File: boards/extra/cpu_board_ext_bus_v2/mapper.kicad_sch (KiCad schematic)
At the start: 3 parts, among them U2 74LS30, U7 74LS30, U8 ATF1502AS-7JX44

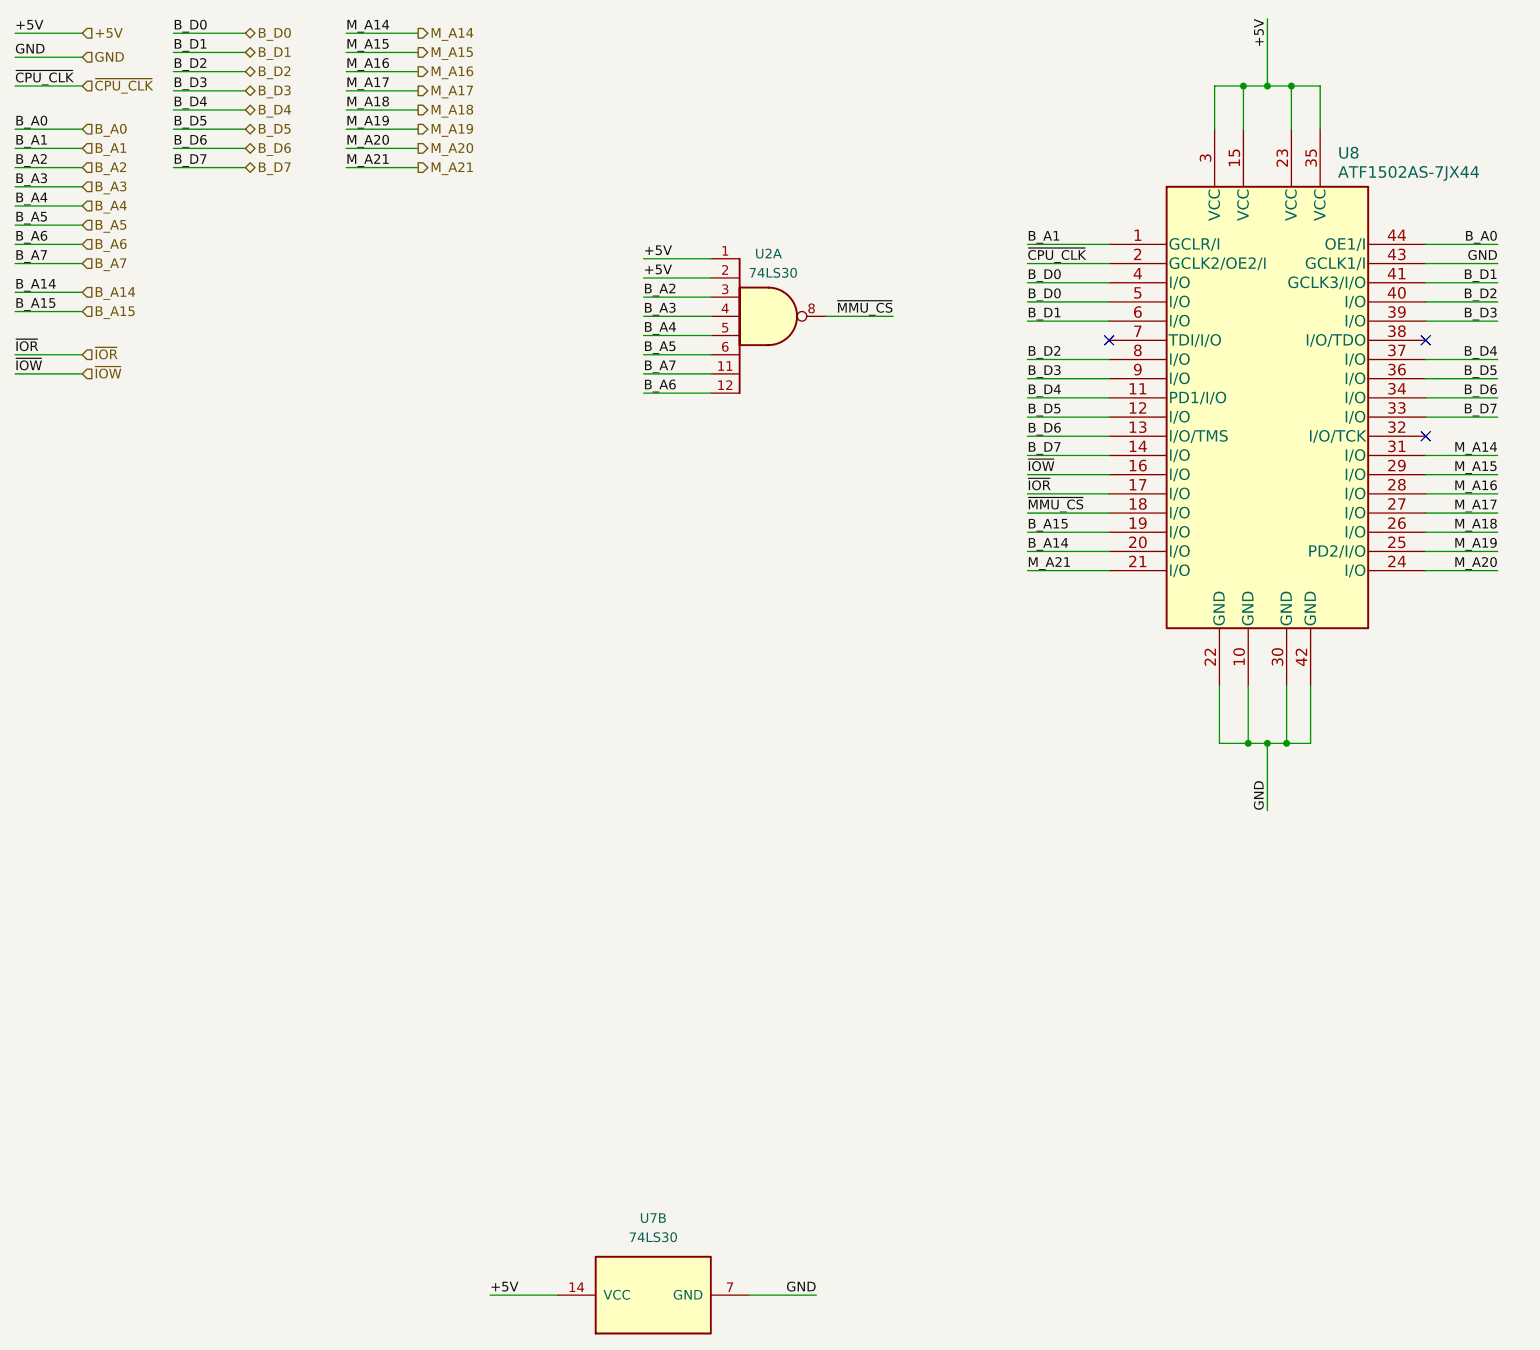
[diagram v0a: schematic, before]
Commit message: Updated CPU board V2 with extension bus
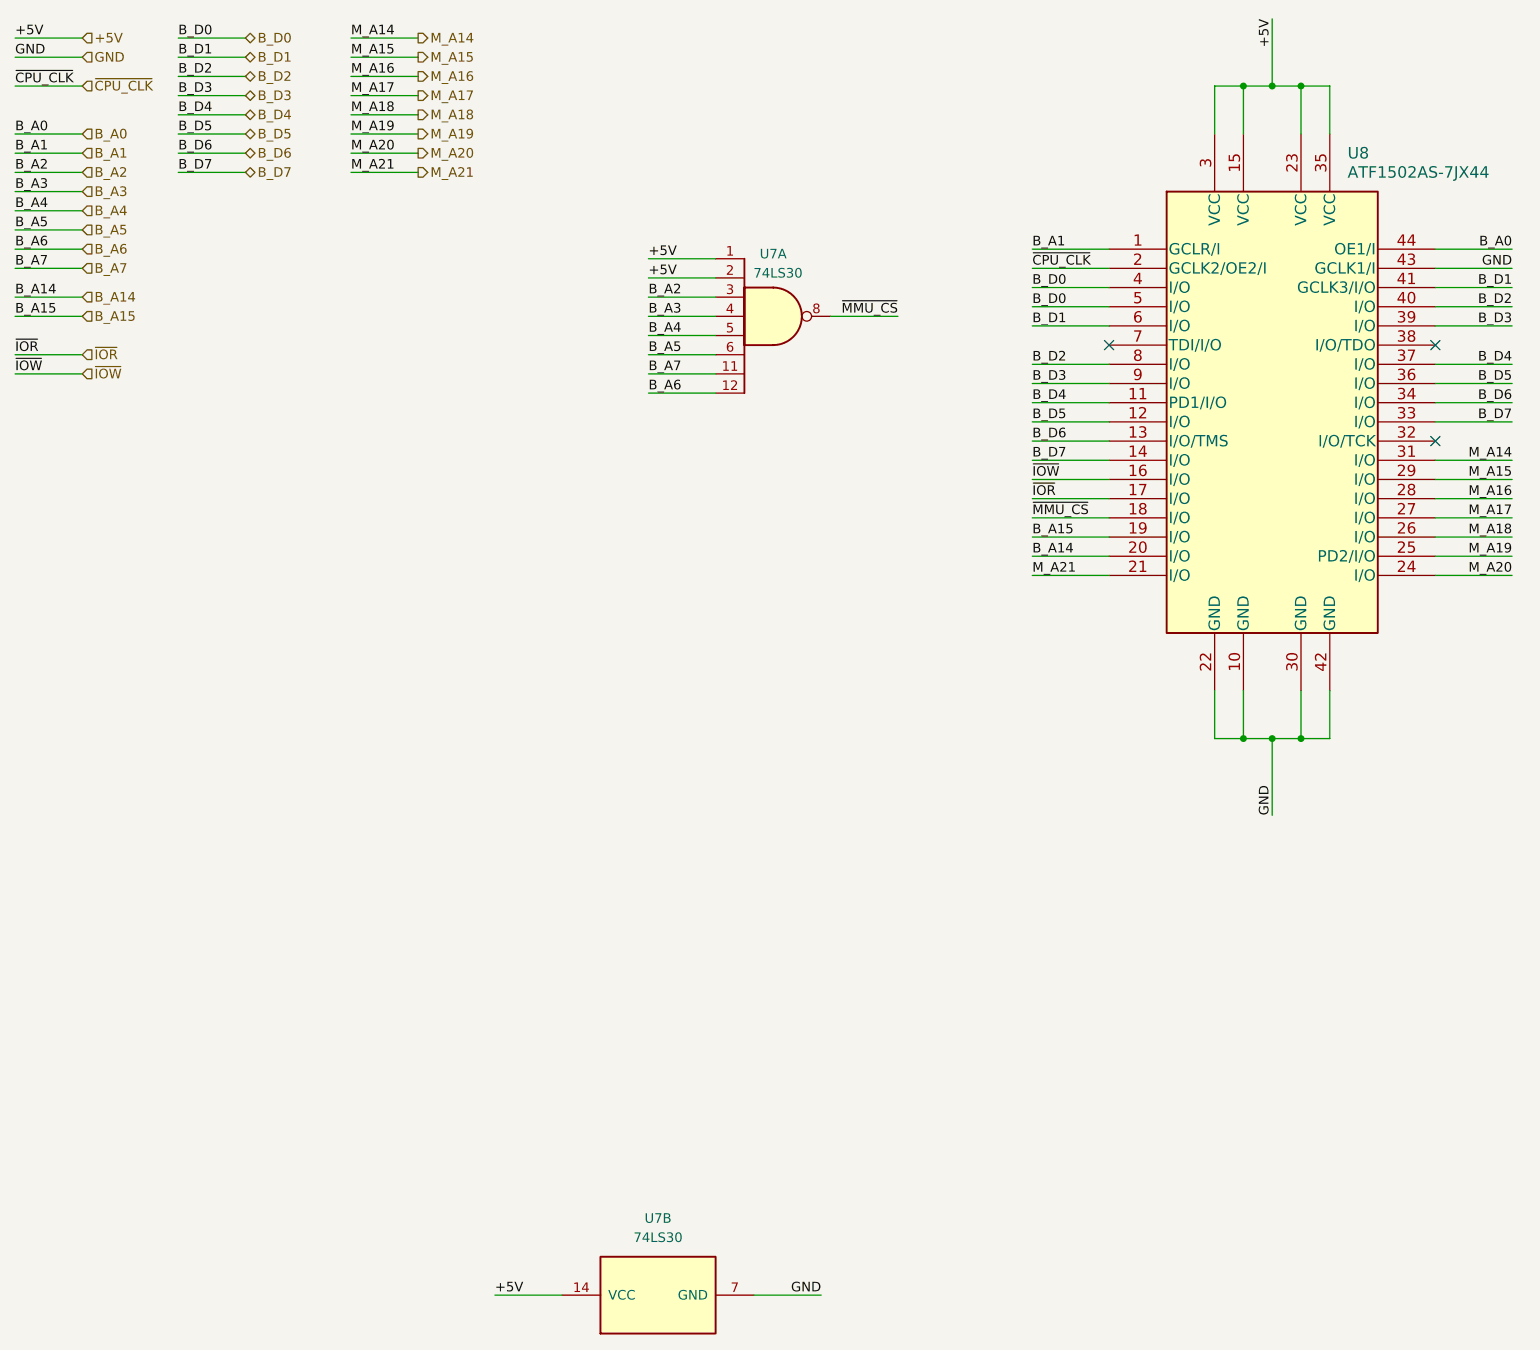
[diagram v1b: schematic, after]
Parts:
- renumbered U2 to U7
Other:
- moved on the sheet: U7A, U7B, U8
